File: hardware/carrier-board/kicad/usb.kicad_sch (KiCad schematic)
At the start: 0 parts

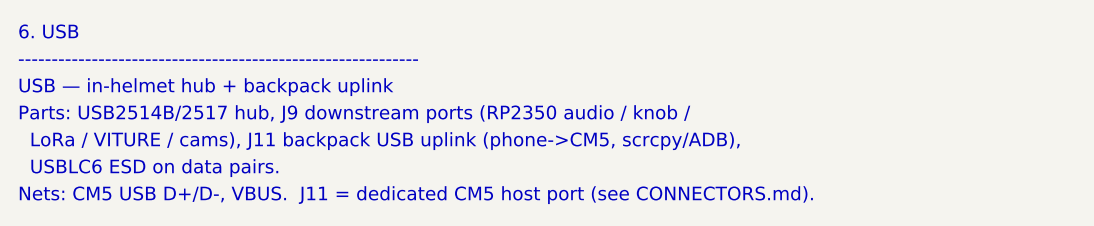
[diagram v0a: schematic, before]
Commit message: Carrier docs + KiCad plan: full two-brain pass (CM5 HUB75 + RP2354B I/O)
Propagate the two-brain architecture across the whole doc set and KiCad plan:
- REQUIREMENTS: restructured M1-M12 (CM5 HUB75; RP2354B core/MAX7219/WS2812/
  sensors/buttons/servos; USB selector + standalone program port); N-list reworked.
- POWER: add +V_SERVO and +3V3_RP rails, servo current budget, updated worked
  total + protection; sensors now on +3V3_RP not CM5 3V3.
- CONNECTORS: J3 re-sourced to RP2354B SPI0, J4 4 WS2812 zones, J5 +SENS_INT,
  J6 BTN1..10, add J12 USB-C, J20-J27 servos, SW1 USB selector, SWD/UART hdrs;
  drop JP1/JP2; fans presented as RP2354B-default-or-CM5 (decision flagged).
- BOM: add RP2354B core, '125/'245 (RP side), USB mux/USB-C/ESD, servo headers,
  +3V3_RP reg; fix '125 double-count and stale HUB75/MAX7219-shared-buffer/JP1.
- MULTI-BACKEND: HUB75+MAX7219 now simultaneous (different brains); firmware
  CompositePanelOutput is the sole remaining blocker.
- IO-EXPANSION: RP2354B is the primary I/O backbone; I2C expanders secondary.
- kicad: 11-sheet plan, stable UUIDs, generator skips populated face_buffer.
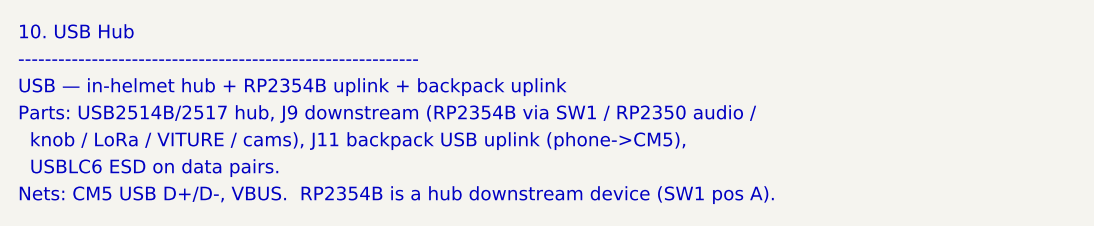
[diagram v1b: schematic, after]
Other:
- note added: "10. USB Hub"
- note added: "Nets: CM5 USB D+/D-, VBUS. RP2354B is a hub downstream device (SW1 pos A)."
- note added: "Parts: USB2514B/2517 hub, J9 downstream (RP2354B via SW1 / RP2350 audio /"
- note added: "USB — in-helmet hub + RP2354B uplink + backpack uplink"
- note added: "knob / LoRa / VITURE / cams), J11 backpack USB uplink (phone->CM5),"
- note removed: "6. USB"
- note removed: "LoRa / VITURE / cams), J11 backpack USB uplink (phone->CM5, scrcpy/ADB),"
- note removed: "Nets: CM5 USB D+/D-, VBUS. J11 = dedicated CM5 host port (see CONNECTORS.md)."
- note removed: "Parts: USB2514B/2517 hub, J9 downstream ports (RP2350 audio / knob /"
- note removed: "USB — in-helmet hub + backpack uplink"
- title: ProtoHUD Carrier — 6. USB -> ProtoHUD Carrier — 10. USB Hub
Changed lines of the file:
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@@
   (paper "A3")
   (title_block
-    (title "ProtoHUD Carrier — 6. USB")
+    (title "ProtoHUD Carrier — 10. USB Hub")
     (rev "A")
     (company "ProtoHUD")
   )
-  (text "6. USB" (at 25.4 25.40 0) (effects (font (size 1.5 1.5)) (justify left bottom)))
+  (text "10. USB Hub" (at 25.4 25.40 0) (effects (font (size 1.5 1.5)) (justify left bottom)))
   (text "------------------------------------------------------------" (at 25.4 28.40 0) (effects (font (size 1.5 1.5)) (justify left bottom)))
-  (text "USB — in-helmet hub + backpack uplink" (at 25.4 31.40 0) (effects (font (size 1.5 1.5)) (justify left bottom)))
-  (text "Parts: USB2514B/2517 hub, J9 downstream ports (RP2350 audio / knob /" (at 25.4 34.40 0) (effects (font (size 1.5 1.5)) (justify left bottom)))
-  (text "  LoRa / VITURE / cams), J11 backpack USB uplink (phone->CM5, scrcpy/ADB)," (at 25.4 37.40 0) (effects (font (size 1.5 1.5)) (justify left bottom)))
+  (text "USB — in-helmet hub + RP2354B uplink + backpack uplink" (at 25.4 31.40 0) (effects (font (size 1.5 1.5)) (justify left bottom)))
+  (text "Parts: USB2514B/2517 hub, J9 downstream (RP2354B via SW1 / RP2350 audio /" (at 25.4 34.40 0) (effects (font (size 1.5 1.5)) (justify left bottom)))
+  (text "  knob / LoRa / VITURE / cams), J11 backpack USB uplink (phone->CM5)," (at 25.4 37.40 0) (effects (font (size 1.5 1.5)) (justify left bottom)))
   (text "  USBLC6 ESD on data pairs." (at 25.4 40.40 0) (effects (font (size 1.5 1.5)) (justify left bottom)))
-  (text "Nets: CM5 USB D+/D-, VBUS.  J11 = dedicated CM5 host port (see CONNECTORS.md)." (at 25.4 43.40 0) (effects (font (size 1.5 1.5)) (justify left bottom)))
+  (text "Nets: CM5 USB D+/D-, VBUS.  RP2354B is a hub downstream device (SW1 pos A)." (at 25.4 43.40 0) (effects (font (size 1.5 1.5)) (justify left bottom)))
   (sheet_instances
     (path "/" (page "1"))
